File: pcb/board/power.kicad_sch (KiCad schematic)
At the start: 30 parts, among them Q1 DMG2305UX, Q2 AO3400A, SW1 PWR, U2 BQ25172, U3 TLV61070A, U4 XC6206P332MR

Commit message: pcb v0.3
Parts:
- added JP4: Jumper_2_Bridged, Jumper:SolderJumper-2_P1.3mm_Bridged_RoundedPad1.0x1.5mm, symbol Jumper:Jumper_2_Bridged
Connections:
- net at SW1.1 (A), U3.3 (EN): now also JP4.2 (B); no longer R23.1
- new net: JP4.1 (A), R23.1
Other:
- moved on the sheet: R23
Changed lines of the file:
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@@
     (stroke (width 0) (type default) (color 0 0 0 0))
   )
-  (wire (pts (xy 99.06 124.46) (xy 99.06 130.81))
+  (wire (pts (xy 99.06 124.46) (xy 99.06 127))
     (stroke (width 0) (type default) (color 0 0 0 0))
   )
@@
     (stroke (width 0) (type default) (color 0 0 0 0))
   )
+  (wire (pts (xy 99.06 138.43) (xy 99.06 137.16))
+    (stroke (width 0) (type default) (color 0 0 0 0))
+  )
   (wire (pts (xy 124.46 45.72) (xy 128.27 45.72))
     (stroke (width 0) (type default) (color 0 0 0 0))
@@
     (stroke (width 0) (type default) (color 0 0 0 0))
   )
-  (wire (pts (xy 99.06 138.43) (xy 99.06 142.24))
+  (wire (pts (xy 99.06 146.05) (xy 99.06 148.59))
     (stroke (width 0) (type default) (color 0 0 0 0))
   )
@@
     )
     (property "Vendor" "C19702" (id 4) (at 182.88 137.16 0)
+      (effects (font (size 1.27 1.27)) hide)
+    )
+    (pin "1")
+    (pin "2")
+  )
+  (symbol (lib_id "Jumper:Jumper_2_Bridged") (at 99.06 132.08 90) (unit 1)
+    (in_bom yes) (on_board yes)
+    (property "Reference" "JP4" (id 0) (at 100.33 132.08 90)
+      (effects (font (size 1.27 1.27)) (justify right))
+    )
+    (property "Value" "Jumper_2_Bridged" (id 1) (at 93.98 124.46 0)
+      (effects (font (size 1.27 1.27)) (justify right) hide)
+    )
+    (property "Footprint" "Jumper:SolderJumper-2_P1.3mm_Bridged_RoundedPad1.0x1.5mm" (id 2) (at 99.06 132.08 0)
+      (effects (font (size 1.27 1.27)) hide)
+    )
+    (property "Datasheet" "~" (id 3) (at 99.06 132.08 0)
       (effects (font (size 1.27 1.27)) hide)
     )
@@
     (pin "2")
   )
-  (symbol (lib_id "power:GND") (at 99.06 142.24 0) (unit 1)
-    (in_bom yes) (on_board yes)
-    (property "Reference" "#PWR011" (id 0) (at 99.06 148.59 0)
-      (effects (font (size 1.27 1.27)) hide)
-    )
-    (property "Value" "GND" (id 1) (at 95.885 141.605 0))
-    (property "Footprint" "" (id 2) (at 99.06 142.24 0)
-      (effects (font (size 1.27 1.27)) hide)
-    )
-    (property "Datasheet" "" (id 3) (at 99.06 142.24 0)
+  (symbol (lib_id "power:GND") (at 99.06 148.59 0) (unit 1)
+    (in_bom yes) (on_board yes)
+    (property "Reference" "#PWR011" (id 0) (at 99.06 154.94 0)
+      (effects (font (size 1.27 1.27)) hide)
+    )
+    (property "Value" "GND" (id 1) (at 95.885 147.955 0))
+    (property "Footprint" "" (id 2) (at 99.06 148.59 0)
+      (effects (font (size 1.27 1.27)) hide)
+    )
+    (property "Datasheet" "" (id 3) (at 99.06 148.59 0)
       (effects (font (size 1.27 1.27)) hide)
     )
@@
     (pin "2")
   )
-  (symbol (lib_id "Device:R") (at 99.06 134.62 0) (unit 1)
-    (in_bom yes) (on_board yes)
-    (property "Reference" "R23" (id 0) (at 96.52 134.62 90)
-      (effects (font (size 1.27 1.27)) (justify left))
-    )
-    (property "Value" "27K" (id 1) (at 99.06 137.16 90)
-      (effects (font (size 1.27 1.27)) (justify left))
-    )
-    (property "Footprint" "Resistor_SMD:R_0603_1608Metric" (id 2) (at 97.282 134.62 90)
-      (effects (font (size 1.27 1.27)) hide)
-    )
-    (property "Datasheet" "~" (id 3) (at 99.06 134.62 0)
-      (effects (font (size 1.27 1.27)) hide)
-    )
-    (property "Vendor" "C22967" (id 4) (at 99.06 134.62 0)
-      (effects (font (size 1.27 1.27)) hide)
-    )
+  (symbol (lib_id "Device:R") (at 99.06 142.24 0) (unit 1)
+    (in_bom yes) (on_board yes)
+    (property "Reference" "R23" (id 0) (at 96.52 142.24 90)
+      (effects (font (size 1.27 1.27)) (justify left))
+    )
+    (property "Value" "27K" (id 1) (at 99.06 143.51 90)
+      (effects (font (size 1.27 1.27)) (justify left))
+    )
+    (property "Footprint" "Resistor_SMD:R_0603_1608Metric" (id 2) (at 97.282 142.24 90)
+      (effects (font (size 1.27 1.27)) hide)
+    )
+    (property "Datasheet" "~" (id 3) (at 99.06 142.24 0)
+      (effects (font (size 1.27 1.27)) hide)
+    )
+    (property "Vendor" "C22967" (id 4) (at 99.06 142.24 0)
+      (effects (font (size 1.27 1.27)) hide)
+    )

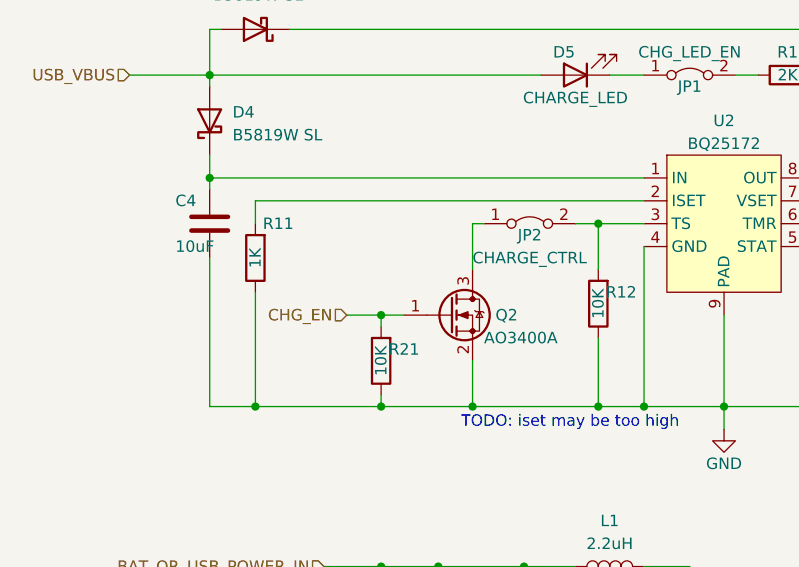
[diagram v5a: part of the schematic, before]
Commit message: update firmware with some v0.3 pcb stuff
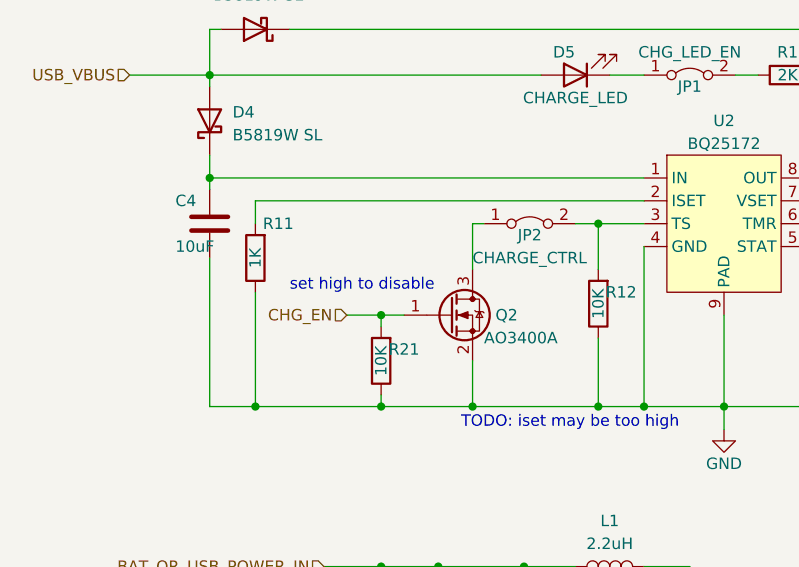
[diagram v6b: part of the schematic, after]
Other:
- note added: "set high to disable"
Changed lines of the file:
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@@
     (stroke (width 0) (type default) (color 0 0 0 0))
+  )
+  (text "set high to disable" (at 88.9 69.85 0)
+    (effects (font (size 1.27 1.27)) (justify left bottom))
   )
   (text "TODO: iset may be too high\n" (at 107.95 85.09 0)
